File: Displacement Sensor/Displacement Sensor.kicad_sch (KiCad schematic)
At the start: 16 parts, among them J1 DTF13-6P, U1 TJA1050DRG, U2 MCP2515-I, X1 ${ALTIUM_VALUE}

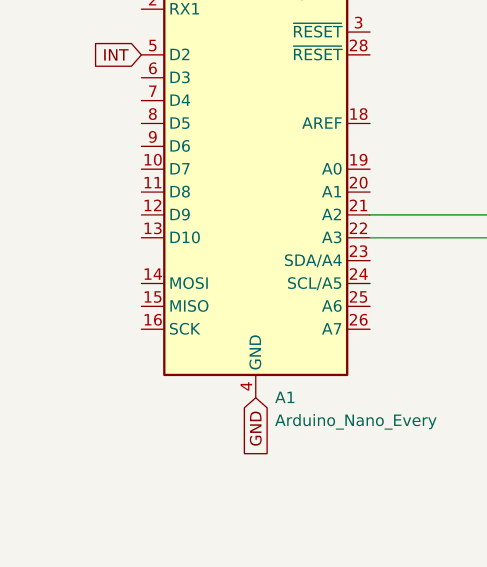
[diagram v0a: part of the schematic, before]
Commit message: Connected Can Bus to Arduino
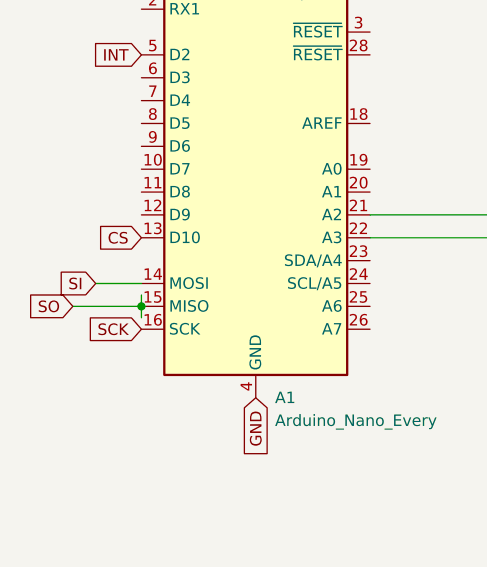
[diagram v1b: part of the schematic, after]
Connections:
- net CS: now also A1.13 (D10)
- net SCK: now also A1.16 (SCK)
- net SI: now also A1.14 (MOSI)
- net SO: now also A1.15 (MISO)
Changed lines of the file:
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@@
+	)
+	(junction
+		(at 54.61 92.71)
+		(diameter 0)
+		(color 0 0 0 0)
 	)
 	(junction
@@
 	(wire
 		(pts
+			(xy 49.53 90.17) (xy 54.61 90.17)
+		)
+		(stroke
+			(width 0)
+			(type default)
+		)
+	)
+	(wire
+		(pts
 			(xy 83.82 162.56) (xy 83.82 148.59)
 		)
@@
 	(wire
 		(pts
+			(xy 46.99 92.71) (xy 54.61 92.71)
+		)
+		(stroke
+			(width 0)
+			(type default)
+		)
+	)
+	(wire
+		(pts
 			(xy 120.65 148.59) (xy 125.73 148.59)
 		)
@@
 	(wire
 		(pts
+			(xy 54.61 93.98) (xy 54.61 92.71)
+		)
+		(stroke
+			(width 0)
+			(type default)
+		)
+	)
+	(wire
+		(pts
 			(xy 226.06 142.24) (xy 222.25 142.24)
 		)
@@
 		)
 	)
+	(wire
+		(pts
+			(xy 54.61 91.44) (xy 54.61 92.71)
+		)
+		(stroke
+			(width 0)
+			(type default)
+		)
+	)
+	(global_label "CS"
+		(shape input)
+		(at 54.61 85.09 180)
+		(fields_autoplaced yes)
+		(effects
+			(font
+				(size 1.27 1.27)
+			)
+			(justify right)
+		)
+		(property "Intersheetrefs" "${INTERSHEET_REFS}"
+			(at 49.1453 85.09 0)
+			(effects
+				(font
+					(size 1.27 1.27)
+				)
+				(justify right)
+				(hide yes)
+			)
+		)
+	)
 	(global_label "Low"
 		(shape input)
@@
 		)
 	)
+	(global_label "SI"
+		(shape input)
+		(at 49.53 90.17 180)
+		(fields_autoplaced yes)
+		(effects
+			(font
+				(size 1.27 1.27)
+			)
+			(justify right)
+		)
+		(property "Intersheetrefs" "${INTERSHEET_REFS}"
+			(at 44.7305 90.17 0)
+			(effects
+				(font
+					(size 1.27 1.27)
+				)
+				(justify right)
+				(hide yes)
+			)
+		)
+	)
 	(global_label "High"
 		(shape input)
@@
 		)
 	)
+	(global_label "SCK"
+		(shape input)
+		(at 54.61 95.25 180)
+		(fields_autoplaced yes)
+		(effects
+			(font
+				(size 1.27 1.27)
+			)
+			(justify right)
+		)
+		(property "Intersheetrefs" "${INTERSHEET_REFS}"
+			(at 47.8753 95.25 0)
+			(effects
+				(font
+					(size 1.27 1.27)
+				)
+				(justify right)
+				(hide yes)
+			)
+		)
+	)
 	(global_label "High"
 		(shape input)
@@
 			(effects
 				(font
+					(size 1.27 1.27)
+				)
+				(justify right)
+				(hide yes)
+			)
+		)
+	)
+	(global_label "SO"
+		(shape input)
+		(at 46.99 92.71 180)
+		(fields_autoplaced yes)
+		(effects
+			(font
+				(size 1.27 1.27)
+			)
+			(justify right)
+		)
+		(property "Intersheetrefs" "${INTERSHEET_REFS}"
+			(at 41.4648 92.71 0)
+			(effects
+				(font

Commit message: AAAAAAAAAA
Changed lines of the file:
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@@
-	)
-	(junction
-		(at 54.61 92.71)
-		(diameter 0)
-		(color 0 0 0 0)
 	)
 	(junction
@@
 	(wire
 		(pts
-			(xy 54.61 93.98) (xy 54.61 92.71)
-		)
-		(stroke
-			(width 0)
-			(type default)
-		)
-	)
-	(wire
-		(pts
 			(xy 226.06 142.24) (xy 222.25 142.24)
 		)
@@
 		)
 		(stroke
-			(width 0)
-			(type default)
-		)
-	)
-	(wire
-		(pts
-			(xy 54.61 91.44) (xy 54.61 92.71)
-		)
-		(stroke
